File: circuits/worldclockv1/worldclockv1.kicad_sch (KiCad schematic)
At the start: 28 parts, among them J1 Power, J2 UART, SW1 EN, SW2 BOOT, U1 LD1117S33TR_SOT223, U2 ESP32-WROOM-32UE, U3 DS3232M

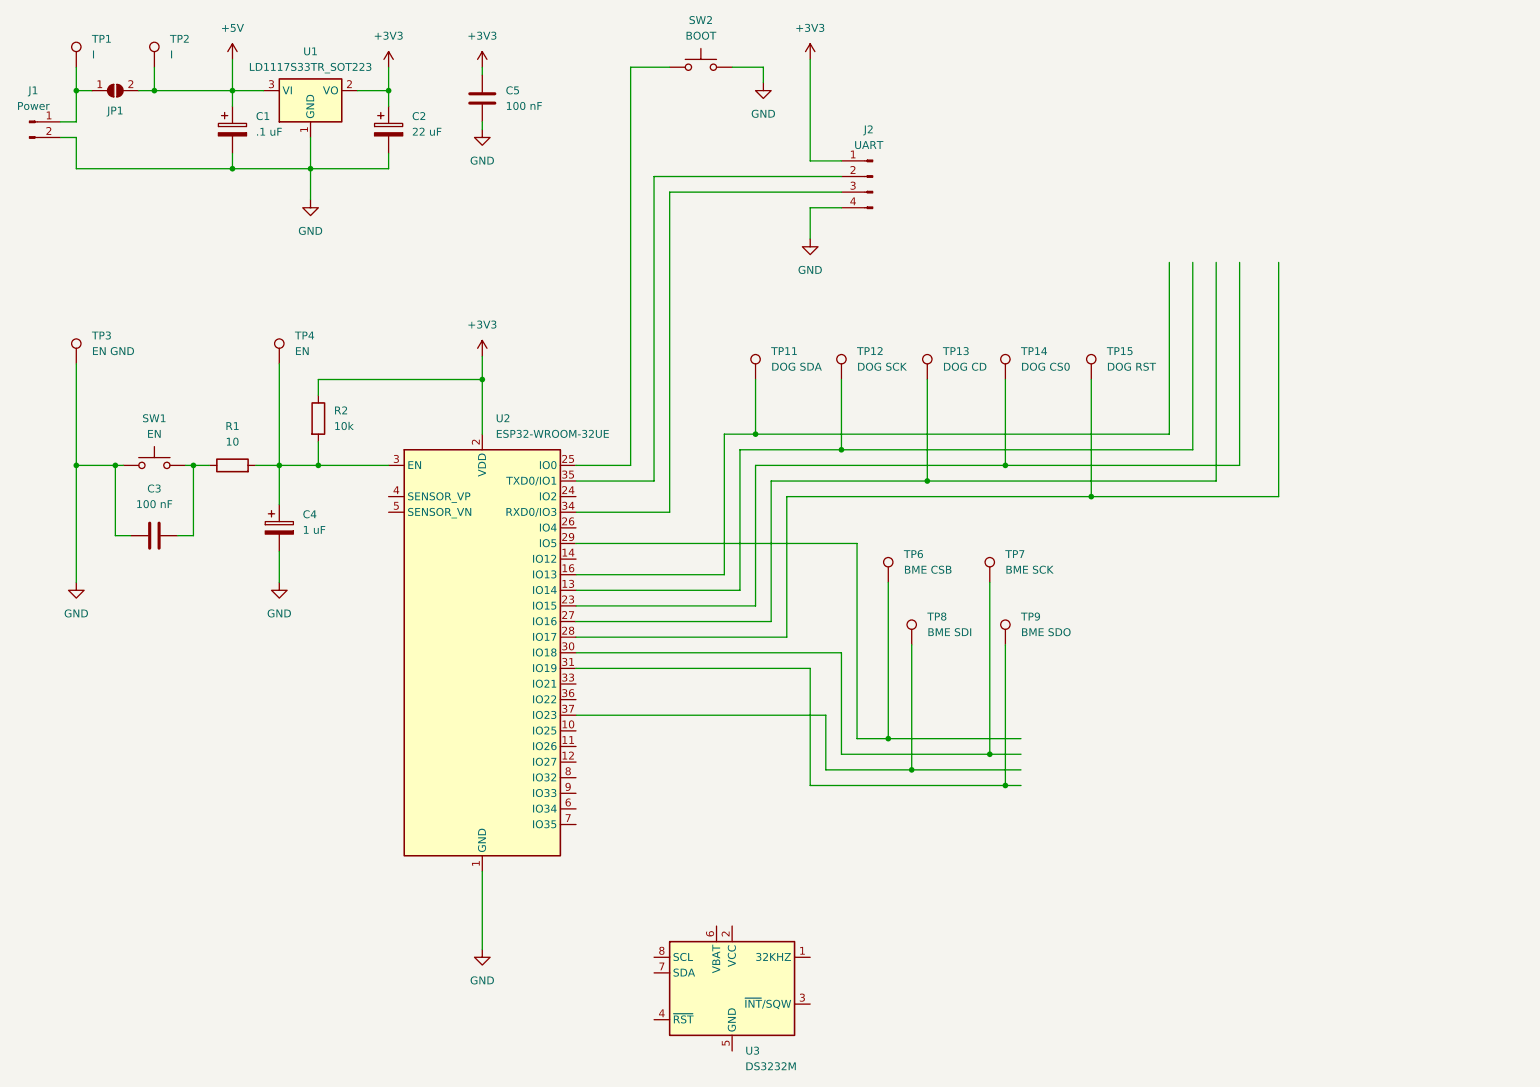
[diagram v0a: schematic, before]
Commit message: World Clock circuit completed. Starting to lay out the PCB.
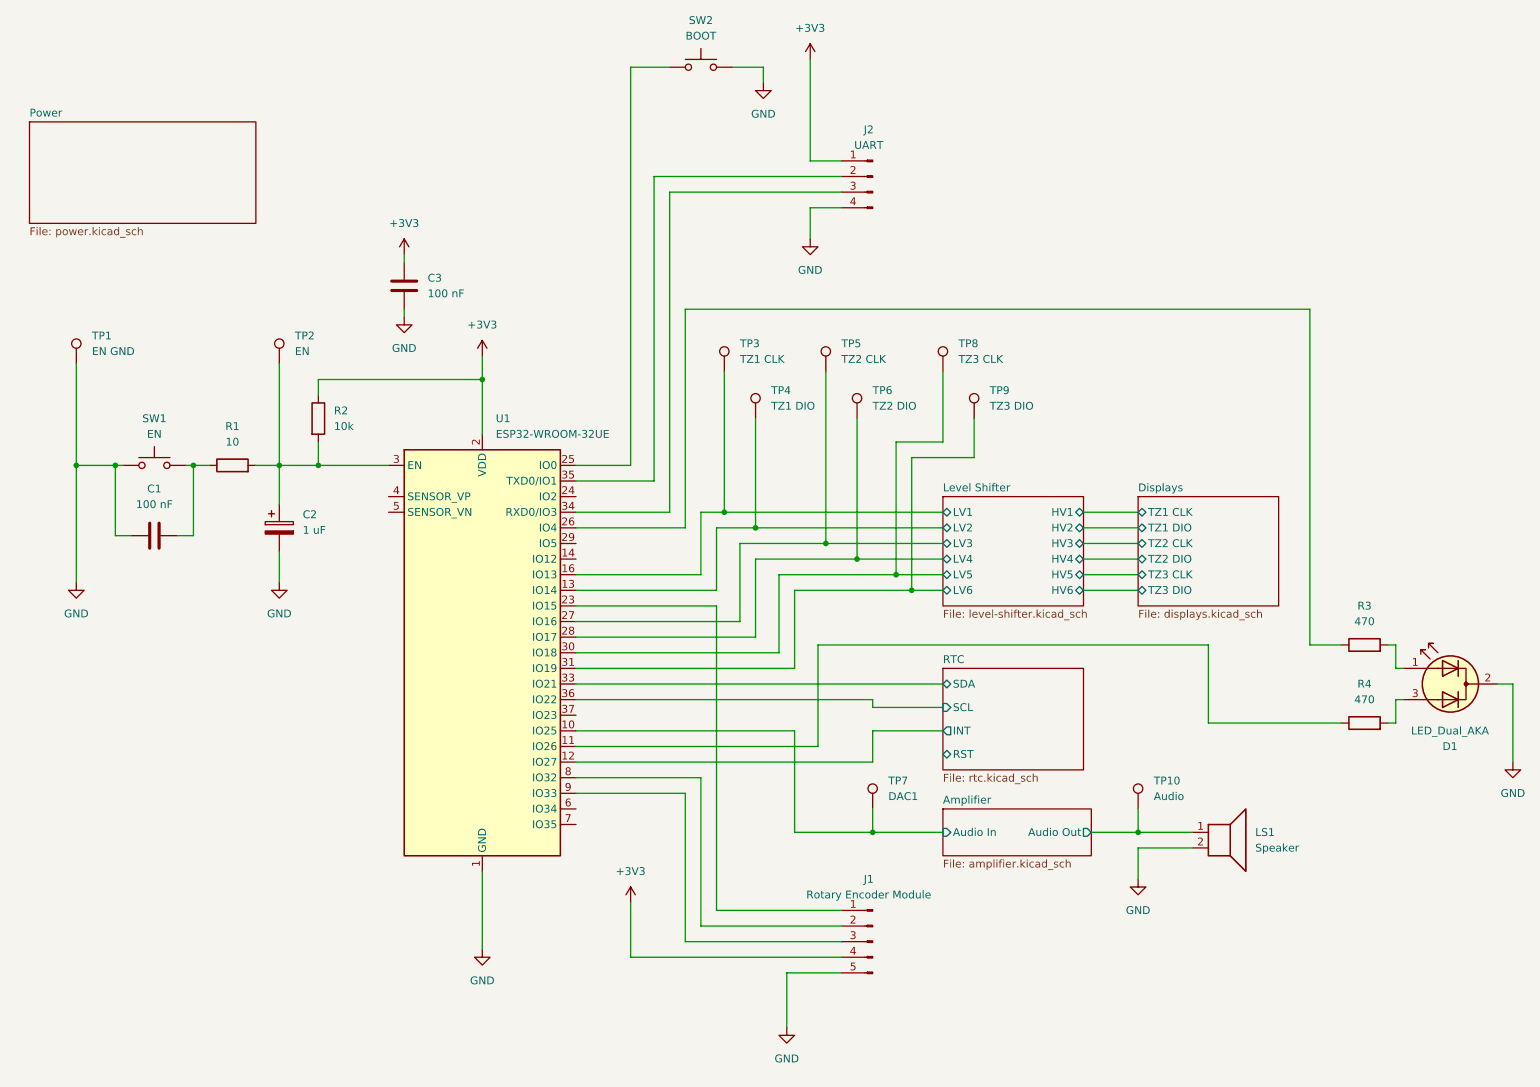
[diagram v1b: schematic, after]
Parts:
- removed C1: .1 uF, Capacitor_SMD:C_1206_3216Metric_Pad1.33x1.80mm_HandSolder, symbol Device:C_Polarized
- removed C2: 22 uF, Capacitor_SMD:CP_Elec_4x5.4, symbol Device:C_Polarized
- removed J1: Power, Connector_PinSocket_2.54mm:PinSocket_1x02_P2.54mm_Vertical, symbol Connector:Conn_01x02_Pin
- removed JP1: ID_WP, Jumper:SolderJumper-2_P1.3mm_Open_RoundedPad1.0x1.5mm, symbol Jumper:SolderJumper_2_Open
- removed TP1, TP2: I, TestPoint:TestPoint_Loop_D2.50mm_Drill1.0mm, symbol Connector:TestPoint
- removed TP6: BME CSB, TestPoint:TestPoint_Loop_D2.50mm_Drill1.0mm, symbol Connector:TestPoint
- removed TP7: BME SCK, TestPoint:TestPoint_Loop_D2.50mm_Drill1.0mm, symbol Connector:TestPoint
- removed U1: LD1117S33TR_SOT223, Package_TO_SOT_SMD:SOT-223-3_TabPin2, symbol Regulator_Linear:LD1117S33TR_SOT223
- removed U3: DS3232M, Package_SO:SOIC-8_3.9x4.9mm_P1.27mm, symbol Timer_RTC:DS3232M
- added D1: LED_Dual_AKA, LED_THT:LED_D3.0mm-3, symbol Device:LED_Dual_AKA
- added J1: Rotary Encoder Module, Connector_PinHeader_2.54mm:PinHeader_1x05_P2.54mm_Vertical, symbol Connector:Conn_01x05_Pin
- added LS1: Speaker, TerminalBlock_MetzConnect:TerminalBlock_MetzConnect_Type055_RT01502HDWU_1x02_P5.00mm_Horizontal, symbol Device:Speaker
- added R3, R4: 470, Resistor_SMD:R_1206_3216Metric_Pad1.30x1.75mm_HandSolder, symbol Device:R
- added TP10: Audio, TestPoint:TestPoint_Loop_D2.50mm_Drill1.0mm, symbol Connector:TestPoint
- TP3: renamed from TP11; value DOG SDA -> TZ1 CLK
- TP4: renamed from TP12; value DOG SCK -> TZ1 DIO
- TP5: renamed from TP8; value BME SDI -> TZ2 CLK
- TP6: renamed from TP9; value BME SDO -> TZ2 DIO
- TP7: renamed from TP15; value DOG RST -> DAC1
- TP8: renamed from TP13; value DOG CD -> TZ3 CLK
- TP9: renamed from TP14; value DOG CS0 -> TZ3 DIO
- renumbered C3 to C1, C4 to C2, C5 to C3, TP3 to TP1, TP4 to TP2, U2 to U1
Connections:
- net +3V3: now also J1.4 (Pin_4)
- net GND: now also D1.2 (K), J1.5 (Pin_5), LS1.2
- net at U1.37 (IO23): no longer TP5.1
- net Level Shifter/LV4: now reaches TP6.1
- net Level Shifter/LV4: now also U1.28 (IO17); no longer U1.31 (IO19)
- net Amplifier/Audio In: now reaches U1.10 (IO25)
- net Amplifier/Audio In: now also TP7.1
- net at U1.11 (IO26): now also R4.1
- net RTC/INT: now reaches U1.12 (IO27)
- net Level Shifter/LV2: now reaches TP4.1, U1.13 (IO14)
- net Level Shifter/LV1: now reaches TP3.1, U1.16 (IO13)
- net at U1.23 (IO15): now also J1.1 (Pin_1); no longer TP9.1
- net at U1.26 (IO4): now also R3.1
- net Level Shifter/LV3: now reaches U1.27 (IO16)
- net Level Shifter/LV3: now also TP5.1; no longer TP8.1
- net Level Shifter/LV5: now reaches U1.30 (IO18)
- net Level Shifter/LV5: now also TP8.1
- net RTC/SDA: now reaches U1.33 (IO21)
- net RTC/SCL: now reaches U1.36 (IO22)
- net at U1.8 (IO32): now also J1.2 (Pin_2)
- net at U1.9 (IO33): now also J1.3 (Pin_3)
- new net: D1.3 (A2), R4.2
- new net: D1.1 (A1), R3.2
- new net Amplifier/Audio Out: LS1.1, TP10.1
- new net Level Shifter/LV6: TP9.1, U1.31 (IO19)
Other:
- added sheet Amplifier (amplifier.kicad_sch)
- added sheet Displays (displays.kicad_sch)
- added sheet Level Shifter (level-shifter.kicad_sch)
- added sheet Power (power.kicad_sch)
- added sheet RTC (rtc.kicad_sch)
- moved on the sheet: C3, TP3, TP4, TP5, TP6, TP7, TP8, TP9

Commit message: World Clock PCB completed
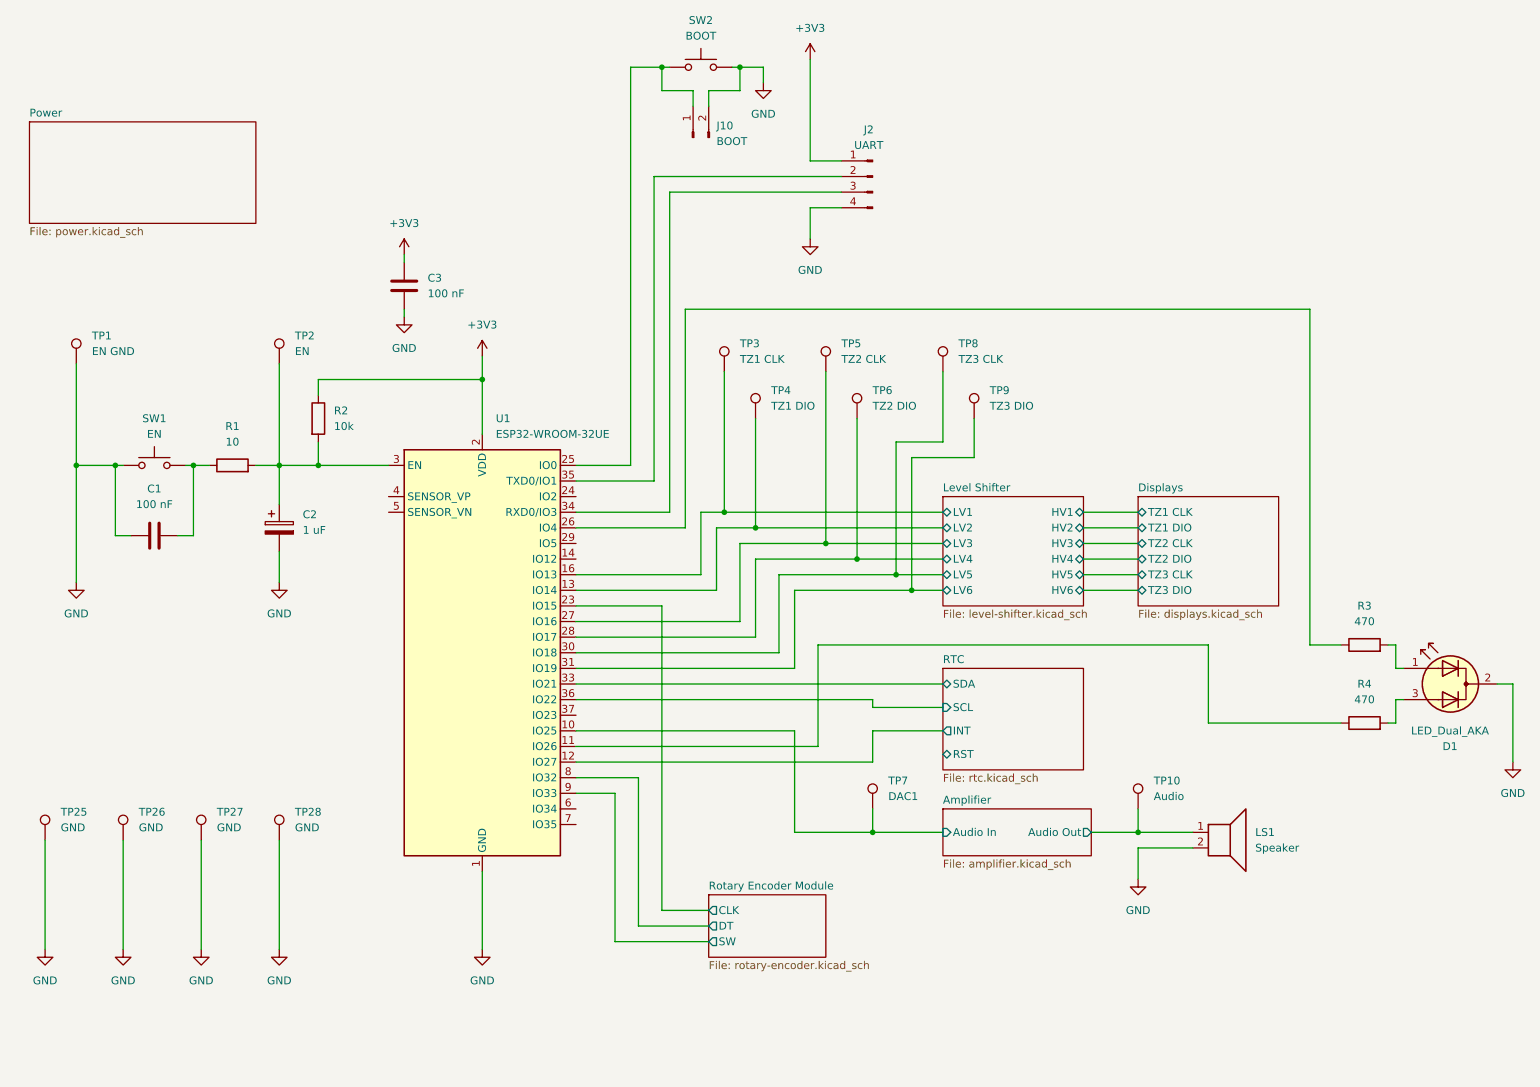
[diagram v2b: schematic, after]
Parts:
- removed J1: Rotary Encoder Module, Connector_PinHeader_2.54mm:PinHeader_1x05_P2.54mm_Vertical, symbol Connector:Conn_01x05_Pin
- added J10: BOOT, Connector_PinHeader_2.54mm:PinHeader_1x02_P2.54mm_Vertical, symbol Connector:Conn_01x02_Pin
- added TP25, TP26, TP27, TP28: GND, TestPoint:TestPoint_Loop_D2.50mm_Drill1.0mm, symbol Connector:TestPoint
- SW1, SW2: footprint Connector_PinSocket_2.54mm:PinSocket_1x02_P2.54mm_Vertical -> Button_Switch_THT:SW_PUSH_6mm
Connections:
- net GND: now also J10.2 (Pin_2), TP25.1, TP26.1, TP27.1, TP28.1
- net Rotary Encoder Module/CLK: now reaches U1.23 (IO15)
- net at SW2.1, U1.25 (IO0): now also J10.1 (Pin_1)
- net Rotary Encoder Module/DT: now reaches U1.8 (IO32)
- net Rotary Encoder Module/SW: now reaches U1.9 (IO33)
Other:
- added sheet Rotary Encoder Module (rotary-encoder.kicad_sch)
